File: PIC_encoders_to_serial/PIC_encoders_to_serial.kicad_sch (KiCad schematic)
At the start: 20 parts, among them J1 Programming, J2 Conn_01x02, J3 Conn_01x04, J4 Conn_01x05, J5 Programming, U1 DSPIC33FJ64MC802-xSP, U2 LM78L33_TO92

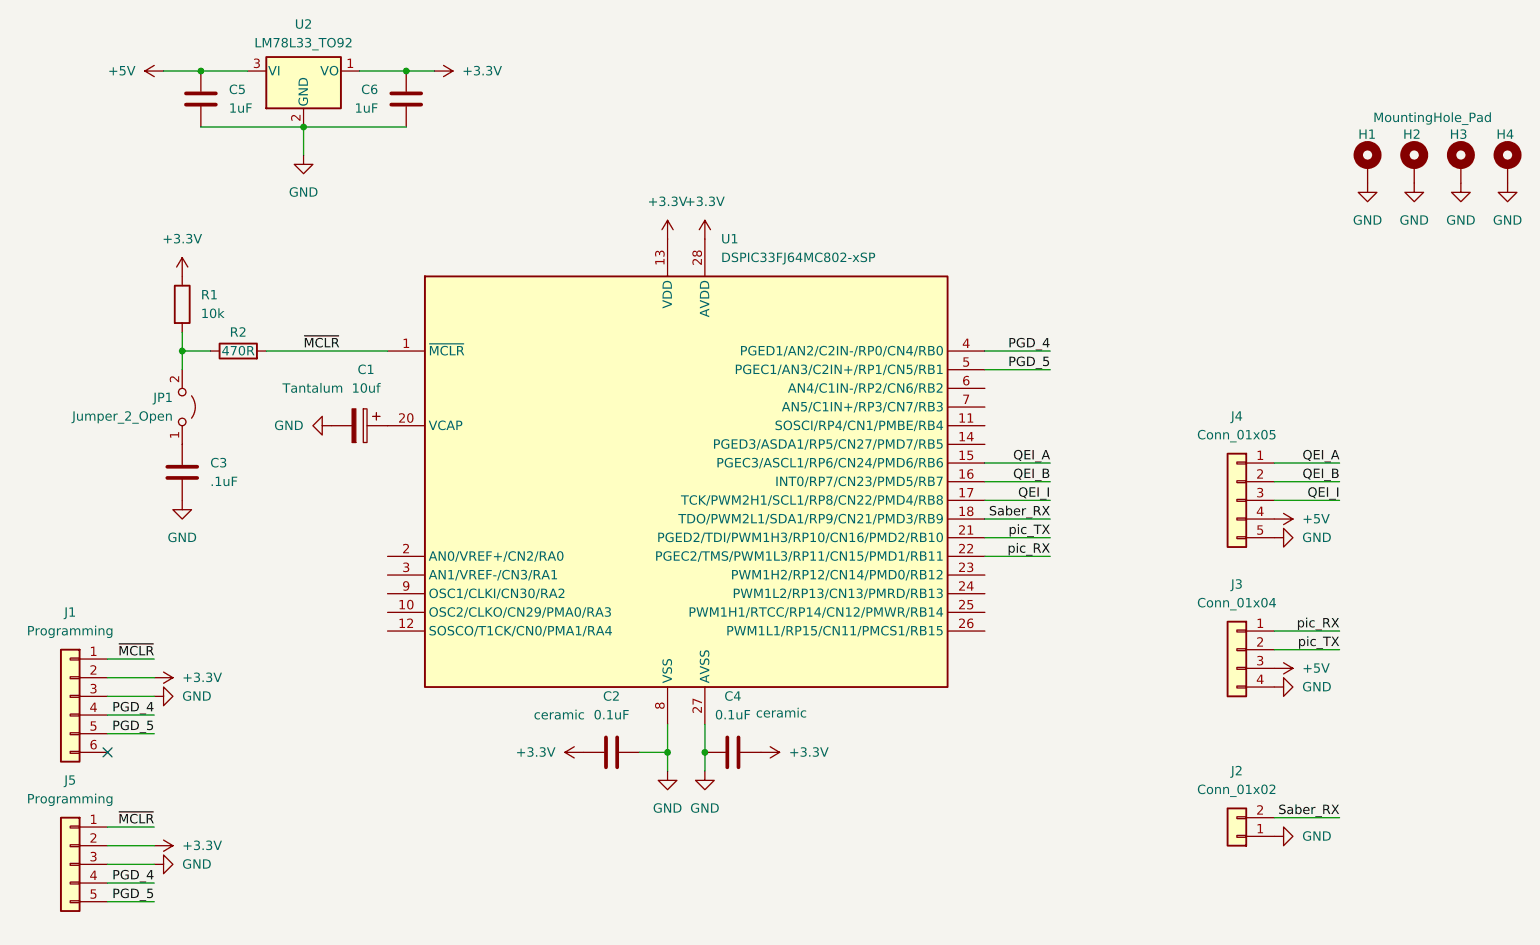
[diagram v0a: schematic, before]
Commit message: changed connectors from JST XH to Molex mini-SPOX
mini-spox is smaller, but retains an almost 2.54mm pitch, so is still somewhat compatible with pin headers if need be
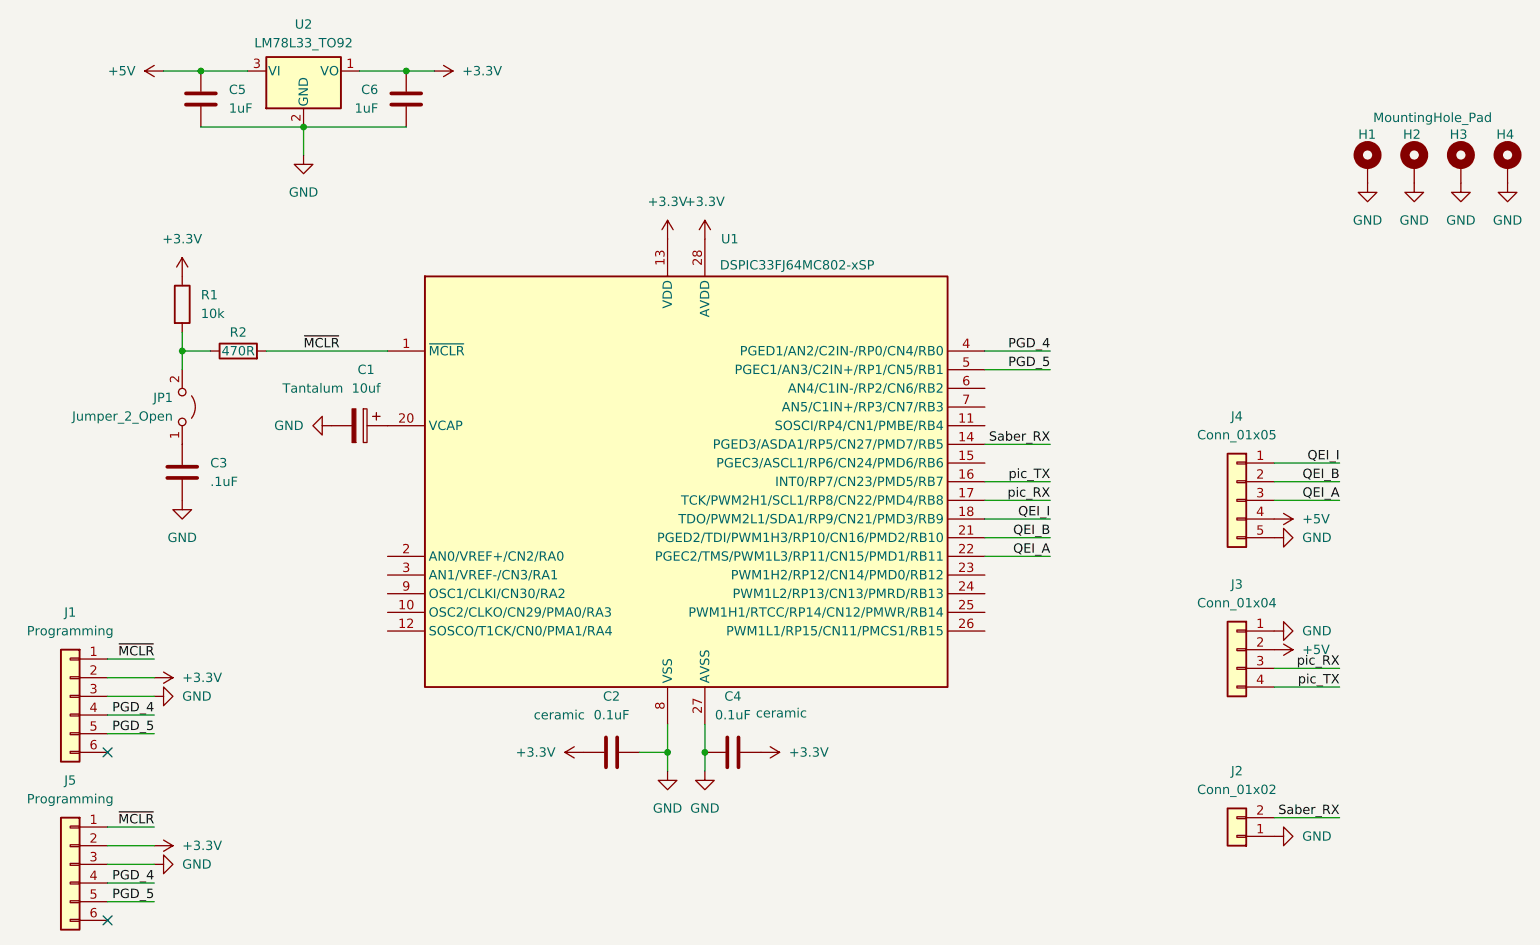
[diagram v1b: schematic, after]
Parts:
- J2: footprint Connector_JST:JST_XH_S2B-XH-A_1x02_P2.50mm_Horizontal -> Connector_Molex:Molex_SPOX_5268-02A_1x02_P2.50mm_Horizontal
- J3: footprint Connector_JST:JST_XH_S4B-XH-A_1x04_P2.50mm_Horizontal -> Connector_Molex:Molex_SPOX_5268-04A_1x04_P2.50mm_Horizontal
- J4: footprint Connector_JST:JST_XH_S5B-XH-A_1x05_P2.50mm_Horizontal -> Connector_Molex:Molex_SPOX_5268-05A_1x05_P2.50mm_Horizontal
- J5: footprint Connector_PinHeader_2.54mm:PinHeader_1x05_P2.54mm_Vertical -> Connector_PinHeader_2.54mm:PinHeader_1x06_P2.54mm_Vertical; symbol Connector_Generic:Conn_01x05 -> Connector_Generic:Conn_01x06
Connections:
- net +5V: now also J3.2 (Pin_2); no longer J3.3 (Pin_3)
- net GND: now also J3.1 (Pin_1); no longer J3.4 (Pin_4)
- net QEI_A: now also J4.3 (Pin_3), U1.22 (PGEC2/TMS/PWM1L3/RP11/CN15/PMD1/RB11); no longer J4.1 (Pin_1), U1.15 (PGEC3/ASCL1/RP6/CN24/PMD6/RB6)
- net QEI_B: now also U1.21 (PGED2/TDI/PWM1H3/RP10/CN16/PMD2/RB10); no longer U1.16 (INT0/RP7/CN23/PMD5/RB7)
- net QEI_I: now also J4.1 (Pin_1), U1.18 (TDO/PWM2L1/SDA1/RP9/CN21/PMD3/RB9); no longer J4.3 (Pin_3), U1.17 (TCK/PWM2H1/SCL1/RP8/CN22/PMD4/RB8)
- net Saber_RX: now also U1.14 (PGED3/ASDA1/RP5/CN27/PMD7/RB5); no longer U1.18 (TDO/PWM2L1/SDA1/RP9/CN21/PMD3/RB9)
- net pic_RX: now also J3.3 (Pin_3), U1.17 (TCK/PWM2H1/SCL1/RP8/CN22/PMD4/RB8); no longer J3.1 (Pin_1), U1.22 (PGEC2/TMS/PWM1L3/RP11/CN15/PMD1/RB11)
- net pic_TX: now also J3.4 (Pin_4), U1.16 (INT0/RP7/CN23/PMD5/RB7); no longer J3.2 (Pin_2), U1.21 (PGED2/TDI/PWM1H3/RP10/CN16/PMD2/RB10)
- no-connect marks 1 -> 2
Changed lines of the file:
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@@
 	)
 	(no_connect
+		(at 31.75 138.43)
+	)
+	(no_connect
 		(at 31.75 115.57)
 	)
@@
 	(wire
 		(pts
-			(xy 151.13 76.2) (xy 160.02 76.2)
+			(xy 151.13 73.66) (xy 160.02 73.66)
 		)
 		(stroke
@@
 	(wire
 		(pts
-			(xy 190.5 99.06) (xy 199.39 99.06)
+			(xy 190.5 104.14) (xy 199.39 104.14)
 		)
 		(stroke
@@
 	(wire
 		(pts
-			(xy 190.5 101.6) (xy 199.39 101.6)
+			(xy 190.5 106.68) (xy 199.39 106.68)
 		)
 		(stroke
@@
 	)
 	(label "QEI_I"
-		(at 160.02 81.28 180)
+		(at 160.02 83.82 180)
 		(fields_autoplaced yes)
 		(effects
@@
 	)
 	(label "Saber_RX"
-		(at 160.02 83.82 180)
+		(at 160.02 73.66 180)
 		(fields_autoplaced yes)
 		(effects
@@
 	)
 	(label "QEI_B"
-		(at 160.02 78.74 180)
+		(at 160.02 86.36 180)
 		(fields_autoplaced yes)
 		(effects
@@
 	)
 	(label "pic_RX"
-		(at 160.02 88.9 180)
+		(at 160.02 81.28 180)
 		(fields_autoplaced yes)
 		(effects
@@
 	)
 	(label "pic_RX"
-		(at 199.39 99.06 180)
+		(at 199.39 104.14 180)
 		(fields_autoplaced yes)
 		(effects
@@
 	)
 	(label "QEI_I"
-		(at 199.39 81.28 180)
+		(at 199.39 76.2 180)
 		(fields_autoplaced yes)
 		(effects
@@
 	)
 	(label "pic_TX"
-		(at 199.39 101.6 180)
+		(at 199.39 106.68 180)
 		(fields_autoplaced yes)
 		(effects
@@
 	)
 	(label "QEI_A"
-		(at 199.39 76.2 180)
+		(at 199.39 81.28 180)
 		(fields_autoplaced yes)
 		(effects
@@
 	)
 	(label "pic_TX"
-		(at 160.02 86.36 180)
+		(at 160.02 78.74 180)
 		(fields_autoplaced yes)
 		(effects
@@
 	)
 	(label "QEI_A"
-		(at 160.02 76.2 180)
+		(at 160.02 88.9 180)
 		(fields_autoplaced yes)
 		(effects
@@
 	(symbol
 		(lib_id "power:GND")
-		(at 190.5 106.68 90)
-		(mirror x)
+		(at 190.5 99.06 90)
 		(unit 1)
 		(exclude_from_sim no)
@@
 		(fields_autoplaced yes)
 		(property "Reference" "#PWR019"
-			(at 196.85 106.68 0)
+			(at 196.85 99.06 0)
 			(effects
 				(font
@@
 		)
 		(property "Value" "GND"
-			(at 194.31 106.6801 90)
+			(at 194.31 99.0599 90)
 			(effects
 				(font
@@
 		)
 		(property "Footprint" ""
-			(at 190.5 106.68 0)
+			(at 190.5 99.06 0)
 			(effects
 				(font
@@
 		)
 		(property "Datasheet" ""
-			(at 190.5 106.68 0)
+			(at 190.5 99.06 0)
 			(effects
 				(font
@@
 		)
 		(property "Description" "Power symbol creates a global label with name \"GND\" , ground"
-			(at 190.5 106.68 0)
+			(at 190.5 99.06 0)
 			(effects
 				(font
@@
 		(on_board yes)
 		(dnp no)
-		(fields_autoplaced yes)
 		(property "Reference" "U1"
 			(at 115.2241 45.72 0)
@@
 		)
 		(property "Value" "DSPIC33FJ64MC802-xSP"
-			(at 115.2241 48.26 0)
+			(at 115.062 49.276 0)
 			(effects
 				(font
@@
 			)
 		)
-		(property "Footprint" "Connector_JST:JST_XH_S4B-XH-A_1x04_P2.50mm_Horizontal"
+		(property "Footprint" "Connector_Molex:Molex_SPOX_5268-04A_1x04_P2.50mm_Horizontal"
 			(at 185.42 101.6 0)
 			(effects
@@
 			)
 		)
-		(property "Footprint" "Connector_JST:JST_XH_S5B-XH-A_1x05_P2.50mm_Horizontal"
+		(property "Footprint" "Connector_Molex:Molex_SPOX_5268-05A_1x05_P2.50mm_Horizontal"
 			(at 185.42 81.28 0)
 			(effects
@@
 	)
 	(symbol
-		(lib_id "Connector_Generic:Conn_01x05")
+		(lib_id "Connector_Generic:Conn_01x06")
 		(at 26.67 130.81 0)
 		(mirror y)
@@
 			)
 		)
-		(property "Footprint" "Connector_PinHeader_2.54mm:PinHeader_1x05_P2.54mm_Vertical"
+		(property "Footprint" "Connector_PinHeader_2.54mm:PinHeader_1x06_P2.54mm_Vertical"
 			(at 26.67 130.81 0)
 			(effects
@@
 			)
 		)
-		(property "Description" "Generic connector, single row, 01x05, script generated (kicad-library-utils/schlib/autogen/connector/)"
+		(property "Description" "Generic connector, single row, 01x06, script generated (kicad-library-utils/schlib/autogen/connector/)"
 			(at 26.67 130.81 0)
 			(effects
@@
 		(pin "2"
 		)
+		(pin "6"
+		)
 		(instances
 			(project ""
@@
 	(symbol
 		(lib_id "power:+5V")
-		(at 190.5 104.14 270)
-		(mirror x)
+		(at 190.5 101.6 270)
 		(unit 1)
 		(exclude_from_sim no)
@@
 		(fields_autoplaced yes)
 		(property "Reference" "#PWR020"
-			(at 186.69 104.14 0)
+			(at 186.69 101.6 0)
 			(effects
 				(font
@@
 		)
 		(property "Value" "+5V"
-			(at 194.31 104.1401 90)
+			(at 194.31 101.5999 90)
 			(effects
 				(font
@@
 		)
 		(property "Footprint" ""
-			(at 190.5 104.14 0)
+			(at 190.5 101.6 0)
 			(effects
 				(font
@@
 		)
 		(property "Datasheet" ""
-			(at 190.5 104.14 0)
+			(at 190.5 101.6 0)
 			(effects
 				(font
@@
 		)
 		(property "Description" "Power symbol creates a global label with name \"+5V\""
-			(at 190.5 104.14 0)
+			(at 190.5 101.6 0)
 			(effects
 				(font
@@
 			)
 		)
-		(property "Footprint" "Connector_JST:JST_XH_S2B-XH-A_1x02_P2.50mm_Horizontal"
+		(property "Footprint" "Connector_Molex:Molex_SPOX_5268-02A_1x02_P2.50mm_Horizontal"
 			(at 185.42 127 0)
 			(effects
